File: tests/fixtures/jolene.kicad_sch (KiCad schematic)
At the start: 83 parts, among them J1 IPEX1, J2 Conn_01x20, J3 Conn_02x02, Q1 BC847C, Q2 BC847C, U1 STM32L073RBT6, U2 TSOP34838, U3 SHT40, U4 MIC5504-3.3YM5, U5 CC1101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

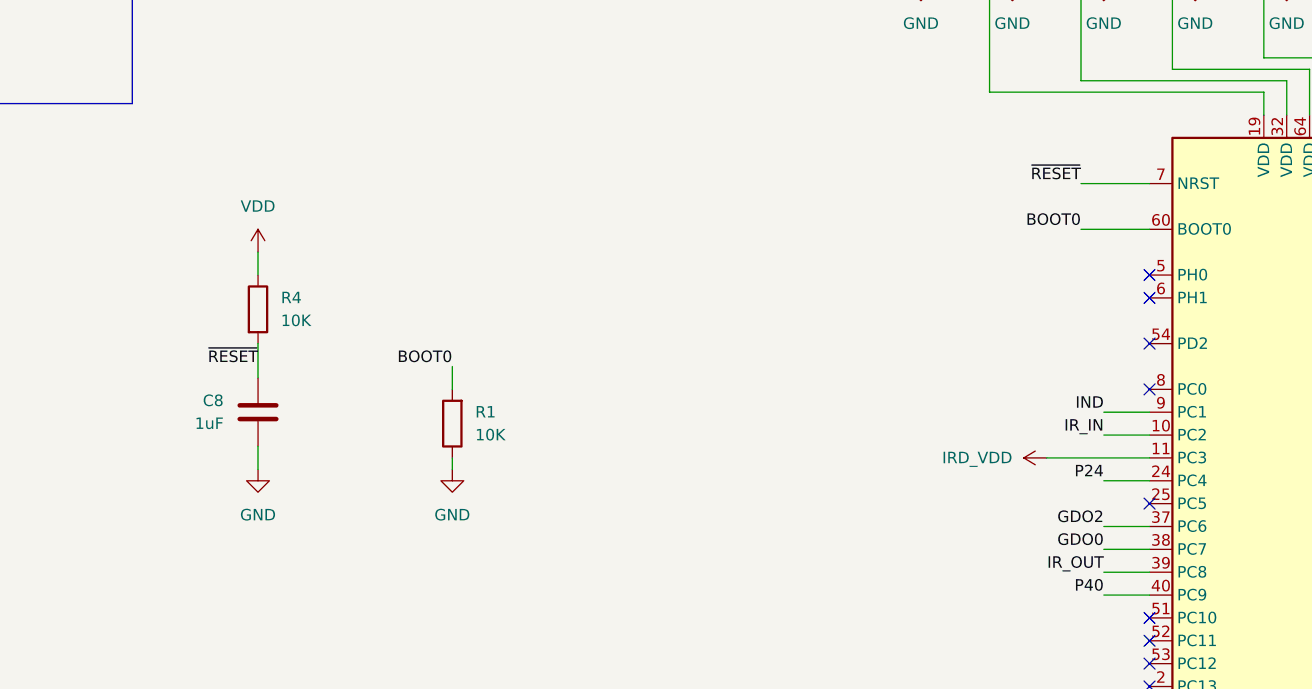
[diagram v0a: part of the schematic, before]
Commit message: Fix mid-line label parsing
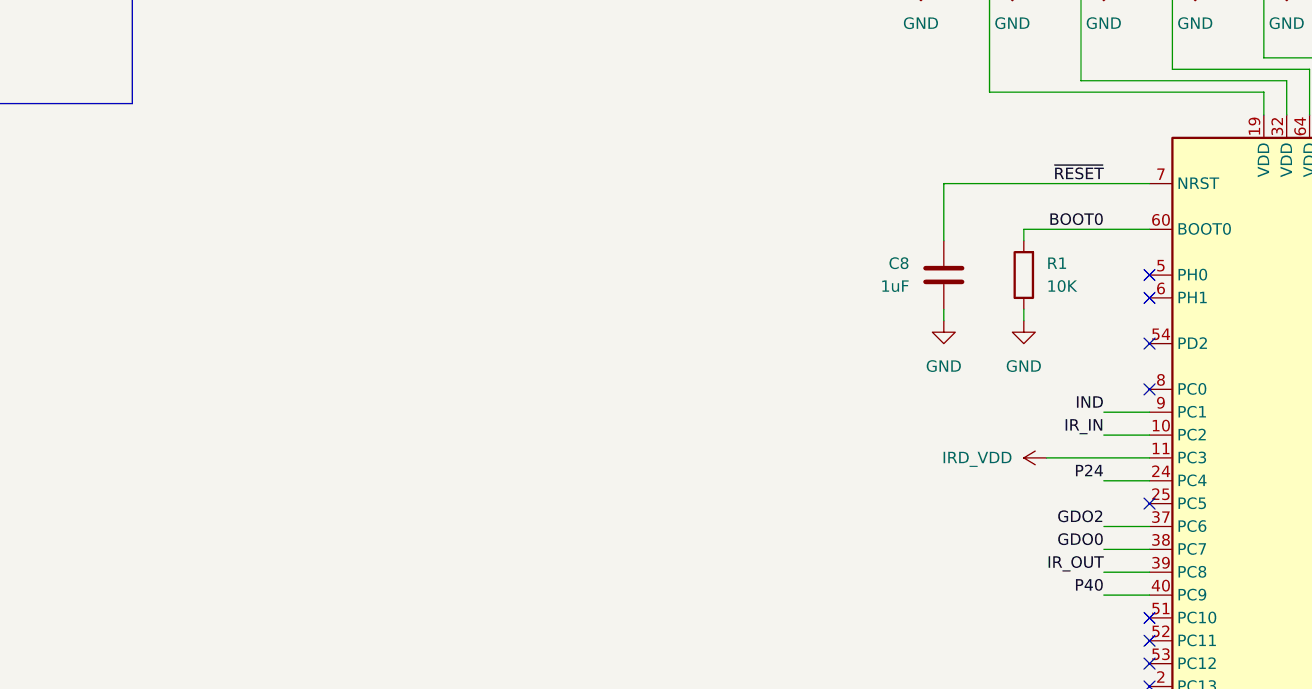
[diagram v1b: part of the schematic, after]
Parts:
- removed R4: 10K, Resistor_SMD:R_0603_1608Metric, symbol Device:R
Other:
- moved on the sheet: C8, R1
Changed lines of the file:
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@@
 	(wire
 		(pts
-			(xy 115.57 92.71) (xy 115.57 95.25)
-		)
-		(stroke
-			(width 0)
-			(type default)
-		)
-	)
-	(wire
-		(pts
 			(xy 227.33 35.56) (xy 227.33 45.72)
 		)
@@
 	(wire
 		(pts
-			(xy 115.57 102.87) (xy 115.57 106.68)
+			(xy 191.77 85.09) (xy 191.77 91.44)
 		)
 		(stroke
@@
 	(wire
 		(pts
-			(xy 137.16 105.41) (xy 137.16 107.95)
+			(xy 200.66 90.17) (xy 200.66 91.44)
 		)
 		(stroke
@@
 	(wire
 		(pts
-			(xy 137.16 116.84) (xy 137.16 115.57)
+			(xy 200.66 100.33) (xy 200.66 99.06)
+		)
+		(stroke
+			(width 0)
+			(type default)
+		)
+	)
+	(wire
+		(pts
+			(xy 191.77 85.09) (xy 214.63 85.09)
 		)
 		(stroke
@@
 	(wire
 		(pts
-			(xy 207.01 90.17) (xy 214.63 90.17)
-		)
-		(stroke
-			(width 0)
-			(type default)
-		)
-	)
-	(wire
-		(pts
 			(xy 374.65 73.66) (xy 381 73.66)
 		)
@@
 	(wire
 		(pts
+			(xy 200.66 90.17) (xy 214.63 90.17)
+		)
+		(stroke
+			(width 0)
+			(type default)
+		)
+	)
+	(wire
+		(pts
 			(xy 240.03 45.72) (xy 237.49 45.72)
 		)
@@
 	(wire
 		(pts
-			(xy 115.57 114.3) (xy 115.57 116.84)
-		)
-		(stroke
-			(width 0)
-			(type default)
-		)
-	)
-	(wire
-		(pts
 			(xy 38.1 82.55) (xy 39.37 82.55)
 		)
@@
 	(wire
 		(pts
-			(xy 207.01 85.09) (xy 214.63 85.09)
-		)
-		(stroke
-			(width 0)
-			(type default)
-		)
-	)
-	(wire
-		(pts
 			(xy 36.83 152.4) (xy 44.45 152.4)
 		)
@@
 	(wire
 		(pts
+			(xy 191.77 100.33) (xy 191.77 99.06)
+		)
+		(stroke
+			(width 0)
+			(type default)
+		)
+	)
+	(wire
+		(pts
 			(xy 396.24 36.83) (xy 406.4 36.83)
 		)
@@
 		)
 	)
-	(label "~{RESET}"
-		(at 115.57 105.41 180)
-		(effects
-			(font
-				(size 1.27 1.27)
-			)
-			(justify right bottom)
-		)
-	)
 	(label "UART2_TX"
 		(at 255.27 90.17 0)
@@
 		)
 	)
-	(label "BOOT0"
-		(at 137.16 105.41 180)
-		(effects
-			(font
-				(size 1.27 1.27)
-			)
-			(justify right bottom)
-		)
-	)
 	(label "IR_OUT"
 		(at 34.29 233.68 180)
@@
 	)
 	(label "~{RESET}"
-		(at 207.01 85.09 180)
+		(at 209.55 85.09 180)
 		(effects
 			(font
@@
 	)
 	(label "BOOT0"
-		(at 207.01 90.17 180)
+		(at 209.55 90.17 180)
 		(effects
 			(font
@@
 	)
 	(symbol
-		(lib_id "Device:R")
-		(at 115.57 99.06 0)
-		(unit 1)
-		(exclude_from_sim no)
-		(in_bom yes)
-		(on_board yes)
-		(dnp no)
-		(fields_autoplaced yes)
-		(property "Reference" "R4"
-			(at 118.11 97.7899 0)
-			(effects
-				(font
-					(size 1.27 1.27)
-				)
-				(justify left)
-			)
-		)
-		(property "Value" "10K"
-			(at 118.11 100.3299 0)
-			(effects
-				(font
-					(size 1.27 1.27)
-				)
-				(justify left)
-			)
-		)
-		(property "Footprint" "Resistor_SMD:R_0603_1608Metric"
-			(at 113.792 99.06 90)
-			(effects
-				(font
-					(size 1.27 1.27)
-				)
-				(hide yes)
-			)
-		)
-		(property "Datasheet" "~"
-			(at 115.57 99.06 0)
-			(effects
-				(font
-					(size 1.27 1.27)
-				)
-				(hide yes)
-			)
-		)
-		(property "Description" "Resistor"
-			(at 115.57 99.06 0)
-			(effects
-				(font
-					(size 1.27 1.27)
-				)
-				(hide yes)
-			)
-		)
-		(pin "2"
-		)
-		(pin "1"
-		)
-		(instances
-			(project ""
-				(path "/59f7a87d-7425-4af0-8212-dc49e6113537"
-					(reference "R4")
-					(unit 1)
-				)
-			)
-		)
-	)
-	(symbol
 		(lib_id "Connector:TestPoint")
 		(at 38.1 97.79 90)
@@
 	(symbol
 		(lib_id "power:GND")
-		(at 115.57 116.84 0)
+		(at 191.77 100.33 0)
 		(unit 1)
 		(exclude_from_sim no)
@@
 		(fields_autoplaced yes)
 		(property "Reference" "#PWR010"
-			(at 115.57 123.19 0)
+			(at 191.77 106.68 0)
 			(effects
 				(font
@@
 		)
 		(property "Value" "GND"
-			(at 115.57 121.92 0)
+			(at 191.77 105.41 0)
 			(effects
 				(font
@@
 		)
 		(property "Footprint" ""
-			(at 115.57 116.84 0)
+			(at 191.77 100.33 0)
 			(effects
 				(font
@@
 		)
 		(property "Datasheet" ""
-			(at 115.57 116.84 0)
+			(at 191.77 100.33 0)
 			(effects
 				(font
@@
 		)
 		(property "Description" "Power symbol creates a global label with name \"GND\" , ground"
-			(at 115.57 116.84 0)
+			(at 191.77 100.33 0)
 			(effects
 				(font
@@
 	)
 	(symbol
-		(lib_id "power:VDD")
-		(at 115.57 92.71 0)
-		(unit 1)
-		(exclude_from_sim no)
-		(in_bom yes)
-		(on_board yes)
-		(dnp no)
-		(fields_autoplaced yes)
-		(property "Reference" "#PWR018"
-			(at 115.57 96.52 0)
-			(effects
-				(font
-					(size 1.27 1.27)
-				)
-				(hide yes)
-			)
-		)
-		(property "Value" "VDD"
-			(at 115.57 87.63 0)
-			(effects
-				(font
-					(size 1.27 1.27)
-				)
-			)
-		)
-		(property "Footprint" ""
-			(at 115.57 92.71 0)
-			(effects
-				(font
-					(size 1.27 1.27)
-				)
-				(hide yes)
-			)
-		)
-		(property "Datasheet" ""
-			(at 115.57 92.71 0)
-			(effects
-				(font
-					(size 1.27 1.27)
-				)
-				(hide yes)
-			)
-		)
-		(property "Description" "Power symbol creates a global label with name \"VDD\""
-			(at 115.57 92.71 0)
-			(effects
-				(font
-					(size 1.27 1.27)
-				)
-				(hide yes)
-			)
-		)
-		(pin "1"
-		)
-		(instances
-			(project "jolene"
-				(path "/59f7a87d-7425-4af0-8212-dc49e6113537"
-					(reference "#PWR018")
-					(unit 1)
-				)
-			)
-		)
-	)
-	(symbol
 		(lib_id "LED:SFH4346")
 		(at 255.27 220.98 90)
@@
 	(symbol
 		(lib_id "power:GND")
-		(at 137.16 116.84 0)
+		(at 200.66 100.33 0)
 		(unit 1)
 		(exclude_from_sim no)
@@
 		(fields_autoplaced yes)
 		(property "Reference" "#PWR029"
-			(at 137.16 123.19 0)
+			(at 200.66 106.68 0)
 			(effects
 				(font
@@
 		)
 		(property "Value" "GND"
-			(at 137.16 121.92 0)
+			(at 200.66 105.41 0)
 			(effects
 				(font
@@
 		)
 		(property "Footprint" ""
-			(at 137.16 116.84 0)
+			(at 200.66 100.33 0)
 			(effects
 				(font
@@
 		)
 		(property "Datasheet" ""
-			(at 137.16 116.84 0)
+			(at 200.66 100.33 0)
 			(effects
 				(font
@@
 		)
 		(property "Description" "Power symbol creates a global label with name \"GND\" , ground"
-			(at 137.16 116.84 0)
+			(at 200.66 100.33 0)
 			(effects
 				(font
@@
 	(symbol
 		(lib_id "Device:R")
-		(at 137.16 111.76 180)
+		(at 200.66 95.25 180)
 		(unit 1)
 		(exclude_from_sim no)
@@
 		(fields_autoplaced yes)
 		(property "Reference" "R1"
-			(at 139.7 110.4899 0)
+			(at 203.2 93.9799 0)
 			(effects
 				(font
@@
 		)
 		(property "Value" "10K"
-			(at 139.7 113.0299 0)
+			(at 203.2 96.5199 0)
 			(effects
 				(font
@@
 		)
 		(property "Footprint" "Resistor_SMD:R_0603_1608Metric"
-			(at 138.938 111.76 90)
+			(at 202.438 95.25 90)
 			(effects
 				(font
@@
 		)
 		(property "Datasheet" "~"
-			(at 137.16 111.76 0)
+			(at 200.66 95.25 0)
 			(effects
 				(font
@@
 		)
 		(property "Description" "Resistor"
-			(at 137.16 111.76 0)
+			(at 200.66 95.25 0)
 			(effects
 				(font
@@
 	(symbol
 		(lib_id "Device:C")
-		(at 115.57 110.49 0)
+		(at 191.77 95.25 0)
 		(mirror y)
 		(unit 1)
@@
 		(dnp no)
 		(property "Reference" "C8"
-			(at 111.76 109.2199 0)
+			(at 187.96 93.9799 0)
 			(effects
 				(font
@@
 		)
 		(property "Value" "1uF"
-			(at 111.76 111.7599 0)
+			(at 187.96 96.5199 0)
 			(effects
 				(font
@@
 		)
 		(property "Footprint" "Capacitor_SMD:C_0603_1608Metric"
-			(at 114.6048 114.3 0)
+			(at 190.8048 99.06 0)
 			(effects
 				(font
@@
 		)
 		(property "Datasheet" "~"
-			(at 115.57 110.49 0)
+			(at 191.77 95.25 0)
 			(effects
 				(font
@@
 		)
 		(property "Description" "Unpolarized capacitor"
-			(at 115.57 110.49 0)
+			(at 191.77 95.25 0)
 			(effects
 				(font
